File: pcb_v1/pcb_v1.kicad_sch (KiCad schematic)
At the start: 29 parts, among them J1 Conn_01x04, P2 BATT, P3 BATT, SW1 RotaryEncoder, SW2 SW_Push, U1 STM32WB5MMG, U2 SRV05-4, U4 TP4057, U5 XC6206P33

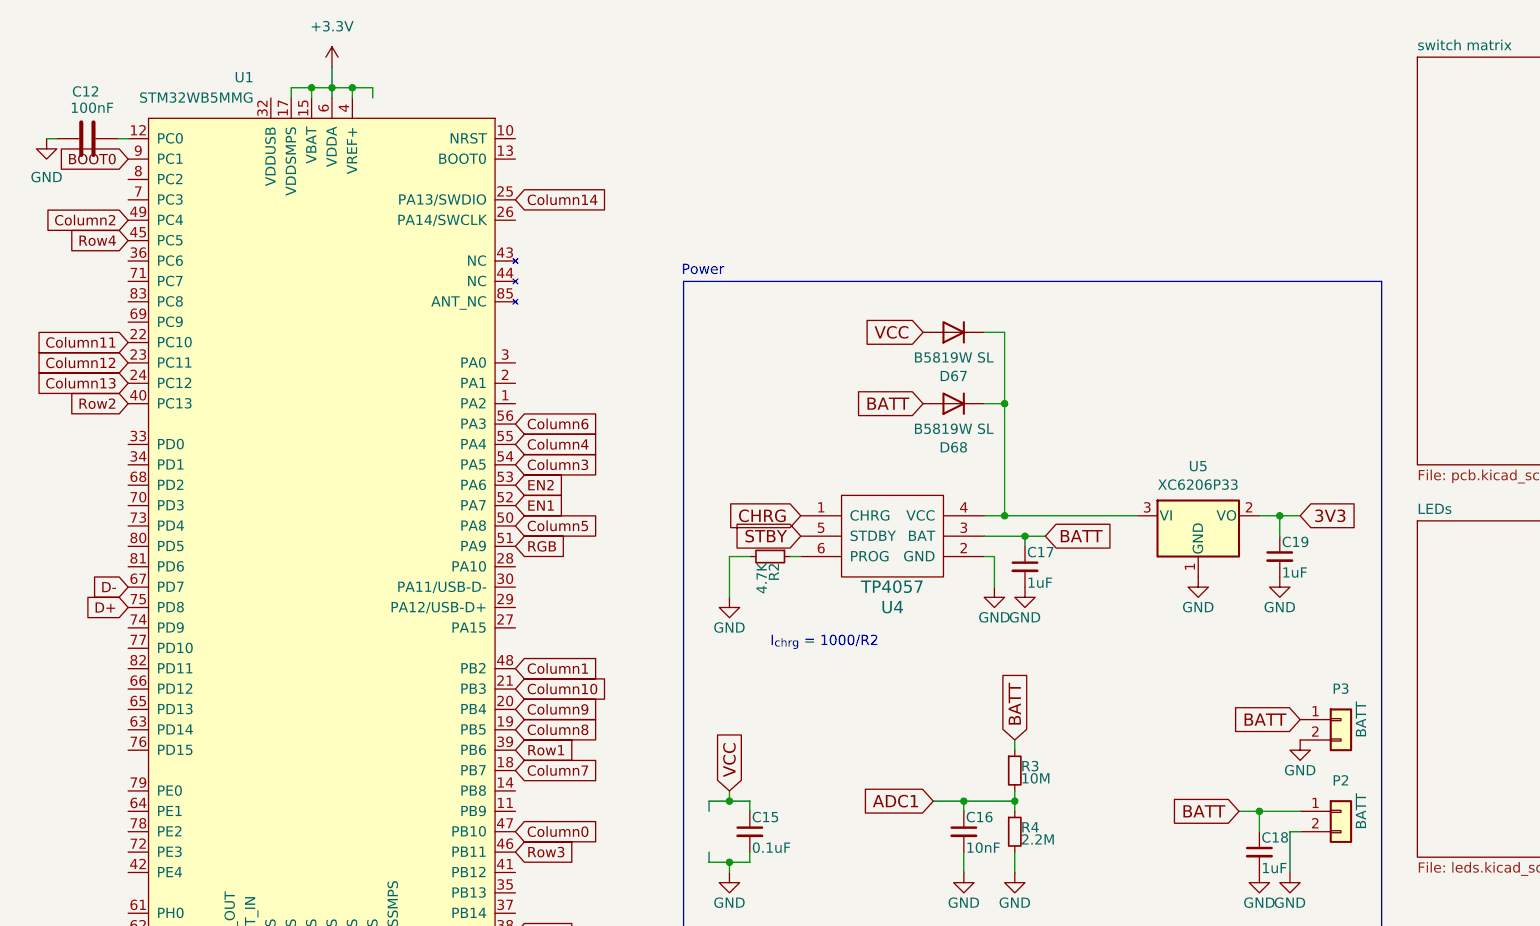
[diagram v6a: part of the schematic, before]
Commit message: Added Decoupling Capacitors
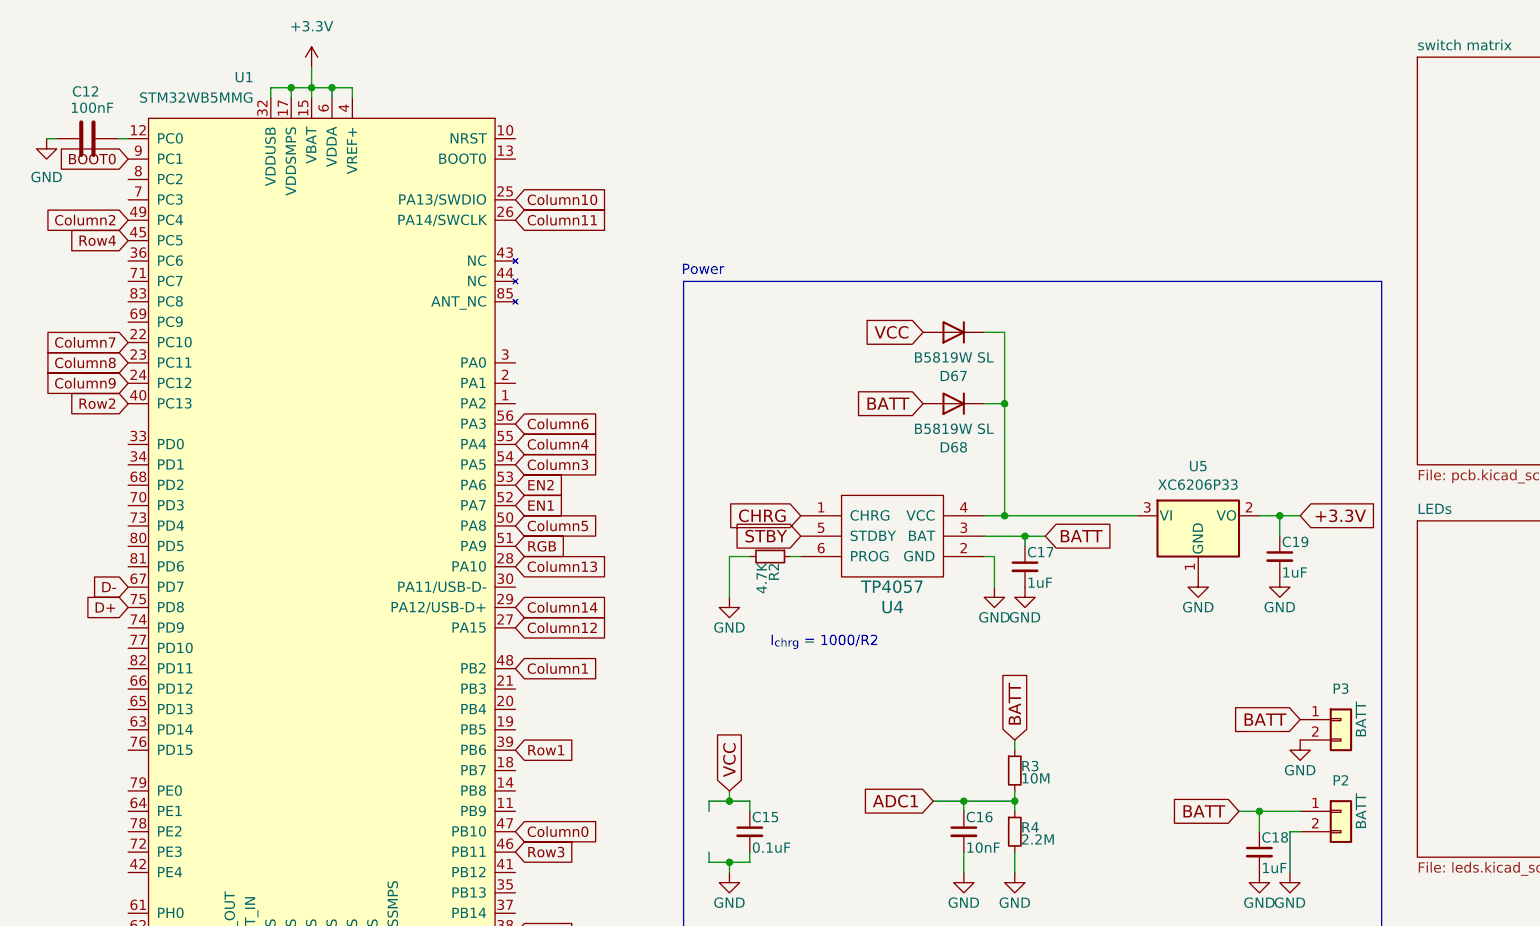
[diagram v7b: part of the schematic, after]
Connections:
- net 3V3 is gone; now on net +3.3V: C19.1, U5.2 (VO)
- net +3.3V: now also U1.32 (VDDUSB)
- net Column10: now also U1.25 (PA13/SWDIO); no longer U1.21 (PB3)
- net Column11: now also U1.26 (PA14/SWCLK); no longer U1.22 (PC10)
- net Column12: now also U1.27 (PA15); no longer U1.23 (PC11)
- net Column13: now also U1.28 (PA10); no longer U1.24 (PC12)
- net Column14: now also U1.29 (PA12/USB-D+); no longer U1.25 (PA13/SWDIO)
- net Column7: now also U1.22 (PC10); no longer U1.18 (PB7)
- net Column8: now also U1.23 (PC11); no longer U1.19 (PB5)
- net Column9: now also U1.24 (PC12); no longer U1.20 (PB4)
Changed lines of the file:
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@@
 	)
 	(junction
-		(at 48.26 22.86)
+		(at 45.72 22.86)
 		(diameter 0)
 		(color 0 0 0 0)
@@
 	)
 	(junction
-		(at 50.8 22.86)
+		(at 48.26 22.86)
 		(diameter 0)
 		(color 0 0 0 0)
 	)
 	(junction
-		(at 53.34 22.86)
+		(at 50.8 22.86)
 		(diameter 0)
 		(color 0 0 0 0)
@@
 	(wire
 		(pts
-			(xy 53.34 22.86) (xy 53.34 24.13)
+			(xy 50.8 22.86) (xy 50.8 24.13)
 		)
 		(stroke
@@
 	(wire
 		(pts
-			(xy 50.8 20.32) (xy 50.8 22.86)
+			(xy 48.26 20.32) (xy 48.26 22.86)
 		)
 		(stroke
@@
 	(wire
 		(pts
-			(xy 55.88 22.86) (xy 55.88 24.13)
+			(xy 53.34 22.86) (xy 53.34 24.13)
 		)
 		(stroke
@@
 	(wire
 		(pts
-			(xy 50.8 22.86) (xy 53.34 22.86)
+			(xy 48.26 22.86) (xy 50.8 22.86)
 		)
 		(stroke
@@
 	(wire
 		(pts
-			(xy 45.72 22.86) (xy 45.72 24.13)
+			(xy 43.18 22.86) (xy 43.18 24.13)
 		)
 		(stroke
@@
 	(wire
 		(pts
-			(xy 53.34 22.86) (xy 55.88 22.86)
+			(xy 50.8 22.86) (xy 53.34 22.86)
 		)
 		(stroke
@@
 	(wire
 		(pts
-			(xy 48.26 22.86) (xy 48.26 24.13)
+			(xy 45.72 22.86) (xy 45.72 24.13)
 		)
 		(stroke
@@
 	(wire
 		(pts
-			(xy 48.26 22.86) (xy 50.8 22.86)
+			(xy 45.72 22.86) (xy 48.26 22.86)
 		)
 		(stroke
@@
 	(wire
 		(pts
-			(xy 45.72 22.86) (xy 48.26 22.86)
+			(xy 43.18 22.86) (xy 45.72 22.86)
 		)
 		(stroke
@@
 	(wire
 		(pts
-			(xy 50.8 22.86) (xy 50.8 24.13)
+			(xy 48.26 22.86) (xy 48.26 24.13)
 		)
 		(stroke
@@
 		)
 	)
+	(global_label "Column11"
+		(shape input)
+		(at 73.66 39.37 0)
+		(fields_autoplaced yes)
+		(effects
+			(font
+				(size 1.27 1.27)
+			)
+			(justify left)
+		)
+		(property "Intersheetrefs" "${INTERSHEET_REFS}"
+			(at 86.1397 39.37 0)
+			(effects
+				(font
+					(size 1.27 1.27)
+				)
+				(justify left)
+				(hide yes)
+			)
+		)
+	)
 	(global_label "D-"
 		(shape input)
@@
 		)
 	)
-	(global_label "3V3"
+	(global_label "+3.3V"
 		(shape input)
 		(at 171.45 76.2 0)
@@
 		)
 	)
-	(global_label "Column9"
-		(shape input)
-		(at 73.66 100.33 0)
-		(fields_autoplaced yes)
-		(effects
-			(font
-				(size 1.27 1.27)
-			)
-			(justify left)
-		)
-		(property "Intersheetrefs" "${INTERSHEET_REFS}"
-			(at 84.9302 100.33 0)
-			(effects
-				(font
-					(size 1.27 1.27)
-				)
-				(justify left)
-				(hide yes)
-			)
-		)
-	)
-	(global_label "Column12"
-		(shape input)
-		(at 25.4 57.15 180)
-		(fields_autoplaced yes)
-		(effects
-			(font
-				(size 1.27 1.27)
-			)
-			(justify right)
-		)
-		(property "Intersheetrefs" "${INTERSHEET_REFS}"
-			(at 12.9203 57.15 0)
-			(effects
-				(font
-					(size 1.27 1.27)
-				)
-				(justify right)
-				(hide yes)
-			)
-		)
-	)
 	(global_label "Column1"
 		(shape input)
@@
 		)
 	)
-	(global_label "Column14"
+	(global_label "Column8"
+		(shape input)
+		(at 25.4 57.15 180)
+		(fields_autoplaced yes)
+		(effects
+			(font
+				(size 1.27 1.27)
+			)
+			(justify right)
+		)
+		(property "Intersheetrefs" "${INTERSHEET_REFS}"
+			(at 14.1298 57.15 0)
+			(effects
+				(font
+					(size 1.27 1.27)
+				)
+				(justify right)
+				(hide yes)
+			)
+		)
+	)
+	(global_label "BOOT0"
+		(shape input)
+		(at 194.31 154.94 90)
+		(fields_autoplaced yes)
+		(effects
+			(font
+				(size 1.27 1.27)
+			)
+			(justify left)
+		)
+		(property "Intersheetrefs" "${INTERSHEET_REFS}"
+			(at 194.31 145.8467 90)
+			(effects
+				(font
+					(size 1.27 1.27)
+				)
+				(justify left)
+				(hide yes)
+			)
+		)
+	)
+	(global_label "Column10"
 		(shape input)
 		(at 73.66 36.83 0)
@@
 		)
 	)
-	(global_label "BOOT0"
+	(global_label "Column13"
 		(shape input)
-		(at 194.31 154.94 90)
+		(at 73.66 82.55 0)
 		(fields_autoplaced yes)
 		(effects
@@
 		)
 		(property "Intersheetrefs" "${INTERSHEET_REFS}"
-			(at 194.31 145.8467 90)
+			(at 86.1397 82.55 0)
 			(effects
 				(font
@@
 		)
 	)
-	(global_label "Column11"
+	(global_label "Column12"
 		(shape input)
-		(at 25.4 54.61 180)
+		(at 73.66 90.17 0)
 		(fields_autoplaced yes)
 		(effects
@@
 				(size 1.27 1.27)
 			)
-			(justify right)
+			(justify left)
 		)
 		(property "Intersheetrefs" "${INTERSHEET_REFS}"
-			(at 12.9203 54.61 0)
+			(at 86.1397 90.17 0)
 			(effects
 				(font
 					(size 1.27 1.27)
 				)
-				(justify right)
+				(justify left)
 				(hide yes)
 			)
@@
 		)
 	)
-	(global_label "Column7"
+	(global_label "Column14"
 		(shape input)
-		(at 73.66 107.95 0)
+		(at 73.66 87.63 0)
 		(fields_autoplaced yes)
 		(effects
@@
 		)
 		(property "Intersheetrefs" "${INTERSHEET_REFS}"
-			(at 84.9302 107.95 0)
+			(at 86.1397 87.63 0)
 			(effects
 				(font
@@
 		)
 	)
-	(global_label "Column13"
-		(shape input)
-		(at 25.4 59.69 180)
-		(fields_autoplaced yes)
-		(effects
-			(font
-				(size 1.27 1.27)
-			)
-			(justify right)
-		)
-		(property "Intersheetrefs" "${INTERSHEET_REFS}"
-			(at 12.9203 59.69 0)
-			(effects
-				(font
-					(size 1.27 1.27)
-				)
-				(justify right)
-				(hide yes)
-			)
-		)
-	)
 	(global_label "Row1"
 		(shape input)
@@
 		)
 	)
-	(global_label "Column8"
+	(global_label "Column9"
 		(shape input)
-		(at 73.66 102.87 0)
+		(at 25.4 59.69 180)
 		(fields_autoplaced yes)
 		(effects
@@
 				(size 1.27 1.27)
 			)
-			(justify left)
+			(justify right)
 		)
 		(property "Intersheetrefs" "${INTERSHEET_REFS}"
-			(at 84.9302 102.87 0)
+			(at 14.1298 59.69 0)
 			(effects
 				(font
 					(size 1.27 1.27)
 				)
-				(justify left)
+				(justify right)
 				(hide yes)
 			)
@@
 		)
 	)
-	(global_label "EN2"
+	(global_label "Column7"
 		(shape input)
-		(at 232.41 160.02 0)
+		(at 25.4 54.61 180)
 		(fields_autoplaced yes)
 		(effects
@@
 				(size 1.27 1.27)
 			)
-			(justify left)
+			(justify right)
 		)
 		(property "Intersheetrefs" "${INTERSHEET_REFS}"
-			(at 239.0842 160.02 0)
+			(at 14.1298 54.61 0)
 			(effects
 				(font
 					(size 1.27 1.27)
 				)
-				(justify left)
+				(justify right)
 				(hide yes)
 			)
 		)
 	)
-	(global_label "EN1"
+	(global_label "EN2"
 		(shape input)
-		(at 73.66 74.93 0)
+		(at 232.41 160.02 0)
 		(fields_autoplaced yes)
 		(effects
@@
 		)
 		(property "Intersheetrefs" "${INTERSHEET_REFS}"
-			(at 80.3342 74.93 0)
+			(at 239.0842 160.02 0)
 			(effects
 				(font
@@
 		)
 	)
-	(global_label "Column10"
+	(global_label "EN1"
 		(shape input)
-		(at 73.66 97.79 0)
+		(at 73.66 74.93 0)
 		(fields_autoplaced yes)
 		(effects
@@
 		)
 		(property "Intersheetrefs" "${INTERSHEET_REFS}"
-			(at 86.1397 97.79 0)
+			(at 80.3342 74.93 0)
 			(effects
 				(font
@@
 	(symbol
 		(lib_id "power:+3.3V")
-		(at 50.8 20.32 0)
+		(at 48.26 20.32 0)
 		(unit 1)
 		(exclude_from_sim no)
@@
 		(fields_autoplaced yes)
 		(property "Reference" "#PWR011"
-			(at 50.8 24.13 0)
+			(at 48.26 24.13 0)
 			(effects
 				(font
@@
 		)
 		(property "Value" "+3.3V"
-			(at 50.8 15.24 0)
+			(at 48.26 15.24 0)
 			(effects
 				(font
@@
 		)
 		(property "Footprint" ""
-			(at 50.8 20.32 0)
+			(at 48.26 20.32 0)
 			(effects
 				(font
@@
 		)
 		(property "Datasheet" ""
-			(at 50.8 20.32 0)
+			(at 48.26 20.32 0)
 			(effects
 				(font
@@
 		)
 		(property "Description" "Power symbol creates a global label with name \"+3.3V\""
-			(at 50.8 20.32 0)
+			(at 48.26 20.32 0)
 			(effects
 				(font

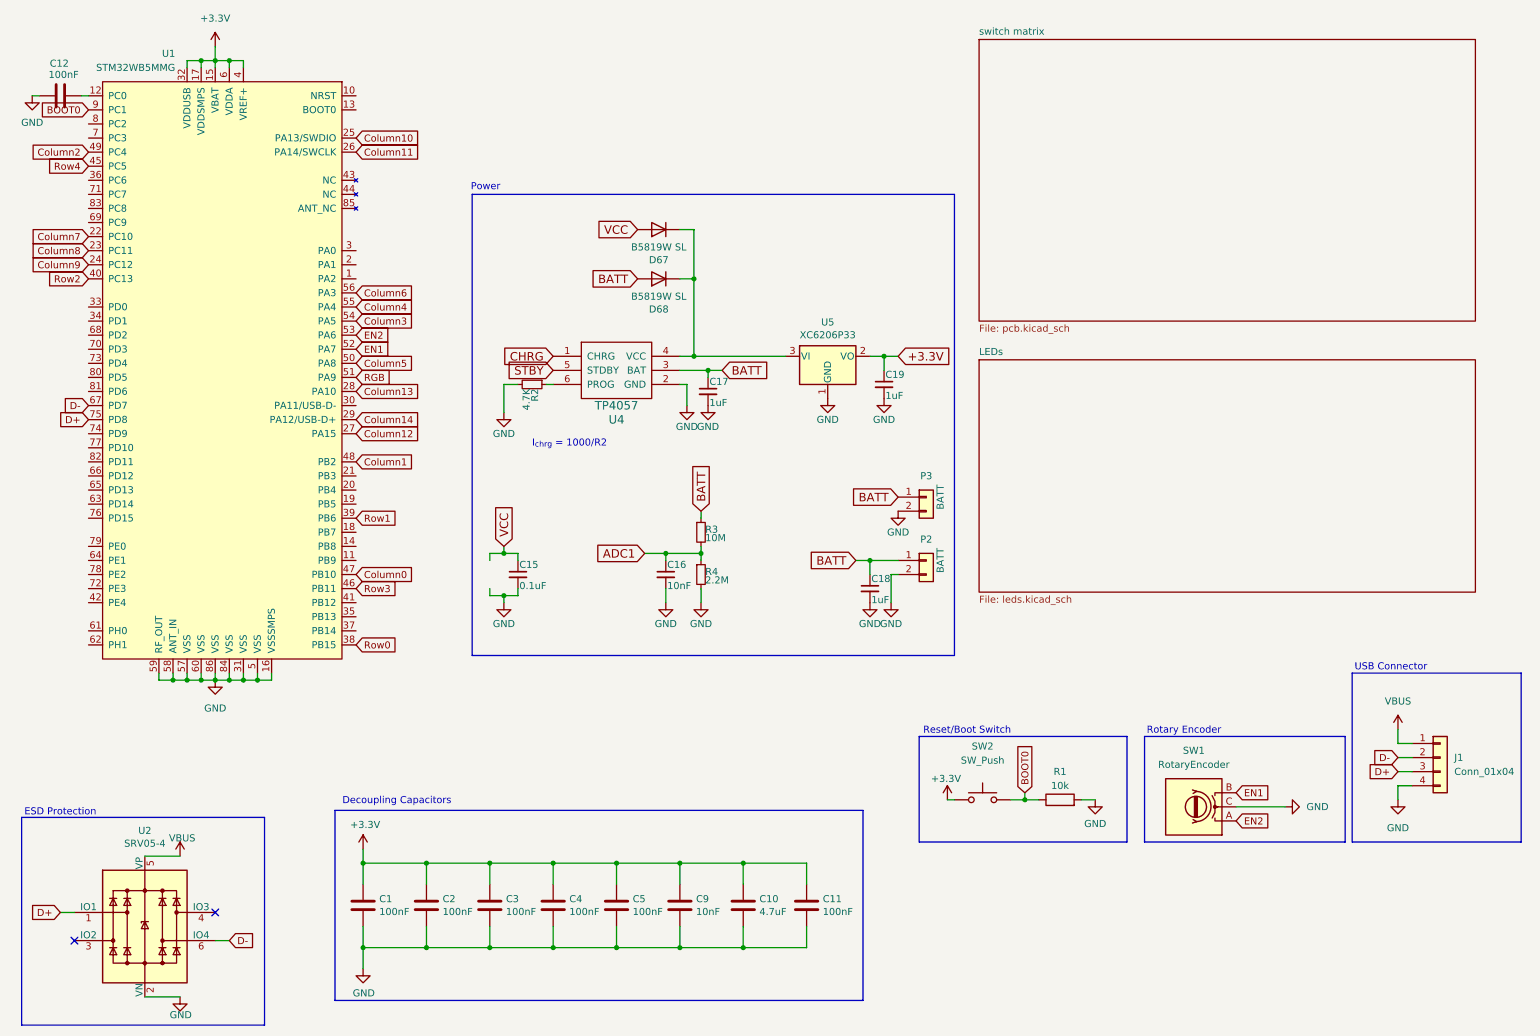
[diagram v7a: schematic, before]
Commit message: Added ESP Protection
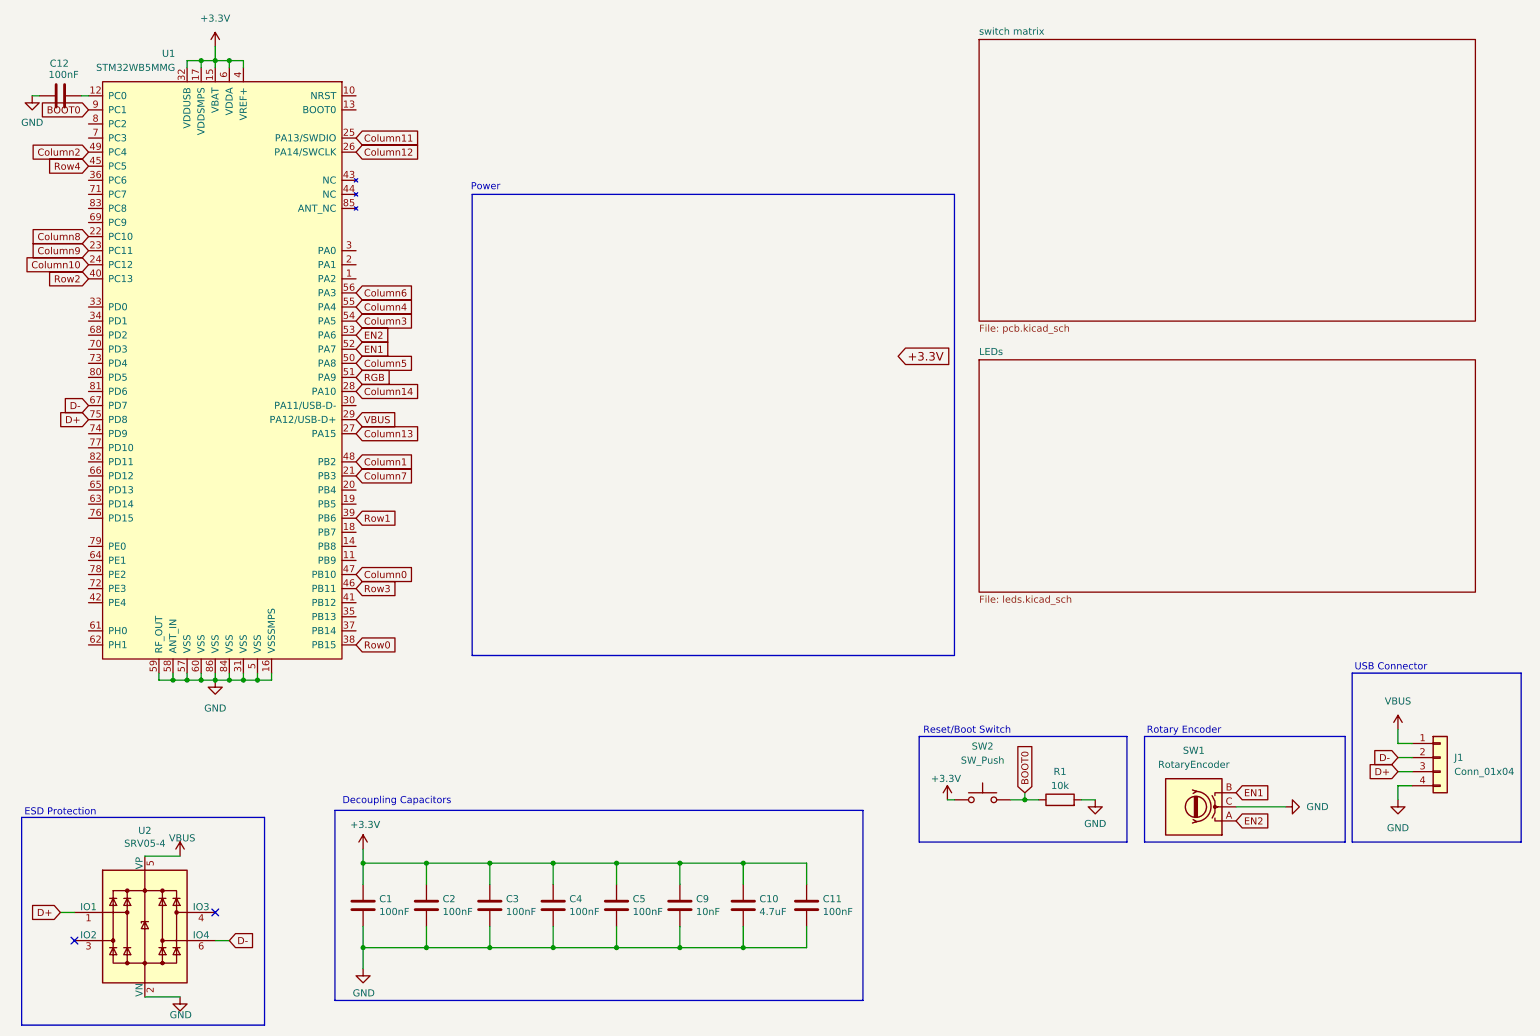
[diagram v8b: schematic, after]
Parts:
- removed C15: 0.1uF, Capacitor_SMD:C_0805_2012Metric, symbol Device:C_Small
- removed C16: 10nF, Capacitor_SMD:C_0805_2012Metric, symbol Device:C_Small
- removed C17, C18, C19: 1uF, Capacitor_SMD:C_0805_2012Metric, symbol Device:C_Small
- removed D67, D68: B5819W SL, Diode_SMD:D_SOD-123, symbol Device:D
- removed P2: BATT, Connector_PinHeader_2.54mm:PinHeader_1x02_P2.54mm_Vertical, symbol Connector_Generic:Conn_01x02
- removed P3: BATT, Connector_PinSocket_2.00mm:PinSocket_1x02_P2.00mm_Vertical, symbol Connector_Generic:Conn_01x02
- removed R2: 4.7K, Resistor_SMD:R_0805_2012Metric, symbol Device:R_Small
- removed R3: 10M, Resistor_SMD:R_0805_2012Metric, symbol Device:R_Small
- removed R4: 2.2M, Resistor_SMD:R_0805_2012Metric, symbol Device:R_Small
- removed U4: TP4057, Package_TO_SOT_SMD:SOT-23-6, symbol custom:TP4057
- removed U5: XC6206P33, Package_TO_SOT_SMD:SOT-23, symbol Regulator_Linear:AP2127N-3.0
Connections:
- net Column10: now also U1.24 (PC12); no longer U1.25 (PA13/SWDIO)
- net Column11: now also U1.25 (PA13/SWDIO); no longer U1.26 (PA14/SWCLK)
- net Column12: now also U1.26 (PA14/SWCLK); no longer U1.27 (PA15)
- net Column13: now also U1.27 (PA15); no longer U1.28 (PA10)
- net Column14: now also U1.28 (PA10); no longer U1.29 (PA12/USB-D+)
- net Column7: now also U1.21 (PB3); no longer U1.22 (PC10)
- net Column8: now also U1.22 (PC10); no longer U1.23 (PC11)
- net Column9: now also U1.23 (PC11); no longer U1.24 (PC12)
- net VBUS: now also U1.29 (PA12/USB-D+)
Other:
- note removed: "I_{chrg} = 1000/R2"
